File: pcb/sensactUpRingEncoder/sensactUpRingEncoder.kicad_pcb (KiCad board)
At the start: 2 copper layers, 45.7 x 39.5 mm, 60 parts, among them J2 IO35, J3 IO36, J32 PROG, J4 ToBase, J6 USB, Q1 IRLML0030, SW4 RESET, U1 ESP32-S3-MINI-1, U12 AHT20, U2 MAX98357A_WLP_Package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

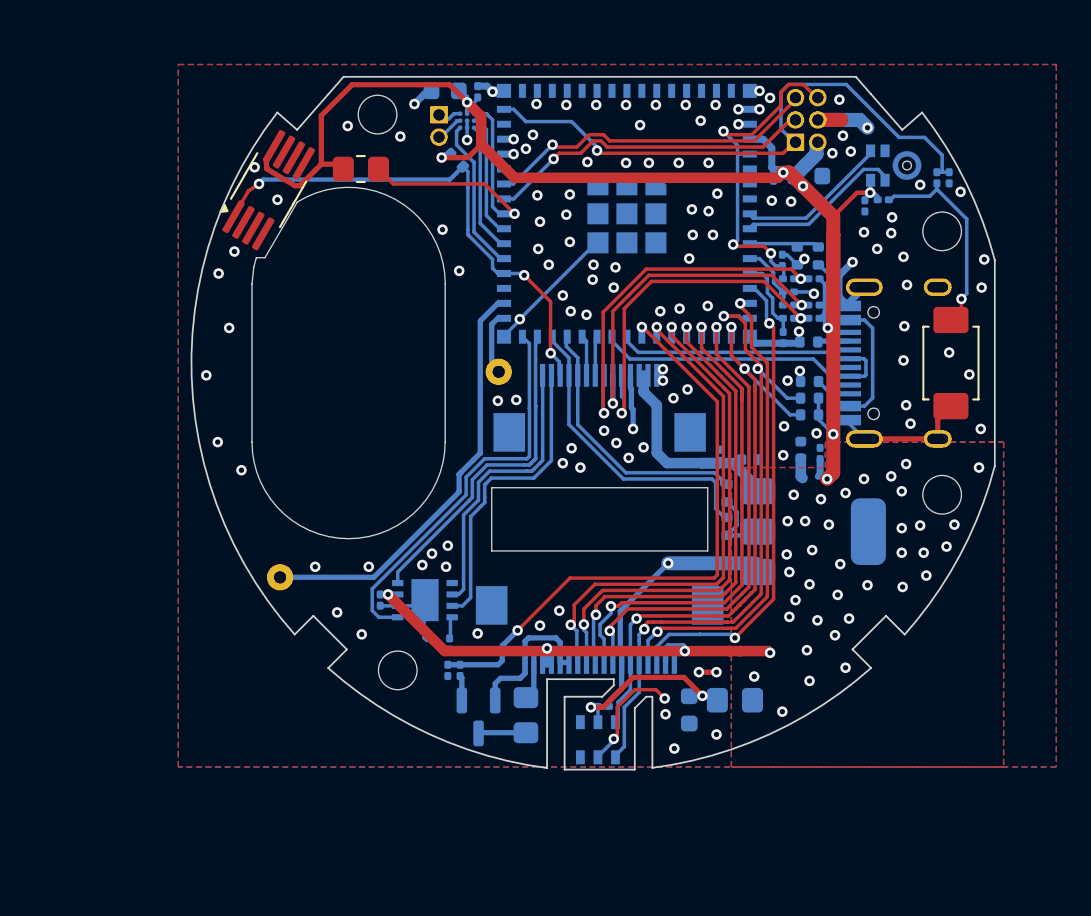
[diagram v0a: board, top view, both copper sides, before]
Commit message: Layout Improvements, added VCML4040
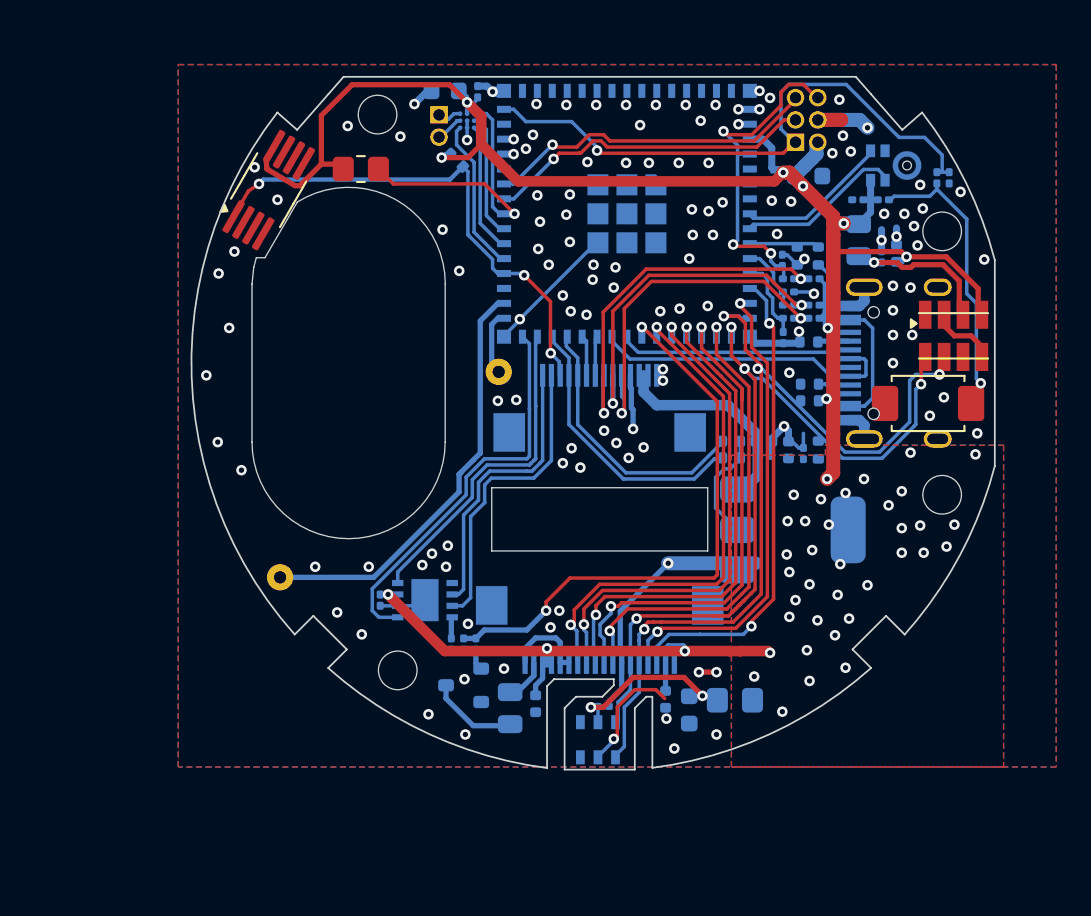
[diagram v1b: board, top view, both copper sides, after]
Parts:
- added C13: 10u, Capacitor_SMD:C_0402_1005Metric, B.Cu at (103.8, 119.2)
- added C14: 10u, Capacitor_SMD:C_0402_1005Metric, B.Cu at (96.3, 119.4)
- added C15: 10u, Capacitor_SMD:C_0402_1005Metric, B.Cu at (116.9, 93.8)
- added C46: u1, Capacitor_SMD:C_0201_0603Metric, B.Cu at (116.0, 94.0)
- added R3: 22R, Resistor_SMD:R_0805_2012Metric, B.Cu at (114.8, 93.0)
- added U5: VCNL4040, liebler_SENSORS:VCNL4040_handsolder, F.Cu at (120.2, 98.5)
- Q1: footprint Package_TO_SOT_SMD:SOT-23 -> liebler_SEMICONDUCTORS:SOT-23_smaller
- R2: value 100R -> 22R; footprint Resistor_SMD:R_0805_2012Metric_Pad1.20x1.40mm_HandSolder -> Resistor_SMD:R_0805_2012Metric
- moved R53 3.91 mm to (107.5, 105.4), turned to 0 degrees
- moved R52 2.96 mm to (107.5, 104.5), turned to 0 degrees
- moved SW4 2.64 mm to (118.7, 102.3), turned to 180 degrees
- moved C10 2.50 mm to (109.4, 105.3), turned to 0 degrees
- moved R51 2.06 mm to (112.5, 105.0), turned to -90 degrees
- moved Q1 1.99 mm to (92.2, 118.3), turned to 180 degrees
- moved R17 1.75 mm to (93.0, 116.0)
- moved R8 1.75 mm to (92.2, 116.0)
- moved C9 1.32 mm to (109.3, 104.5)
- moved U4 1.15 mm to (111.0, 109.5)
- moved R2 0.98 mm to (94.9, 119.7)
- moved C11 0.95 mm to (111.6, 105.2)
- moved C12 0.70 mm to (110.8, 105.0)
- moved C40 0.53 mm to (114.7, 90.7), turned to 180 degrees
- moved R15 0.15 mm to (112.0, 101.2)
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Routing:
- net SDA: track 37.3 -> 51.0 mm, vias 3 -> 4
- net +3V3: track 116.4 -> 129.7 mm, vias 48 -> 47
- net SCL: track 34.3 -> 46.2 mm, vias 3 -> 4
- net Net-(U5-VDD): track 0.00 -> 8.53 mm, vias 0 -> 1
- net GND: track 72.8 -> 65.1 mm
- net Net-(R47-Pad1): track 10.9 -> 15.3 mm
- net Net-(U5-LED_K): track 0.00 -> 2.65 mm
- net Net-(Q1-D): track 2.66 -> 5.04 mm
- net LCD_BL: track 34.4 -> 32.7 mm
- net SDA_EXT: track 17.1 -> 15.7 mm
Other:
- outline, holes or cut-outs redrawn

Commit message: Various updates in sensactRingEncoder
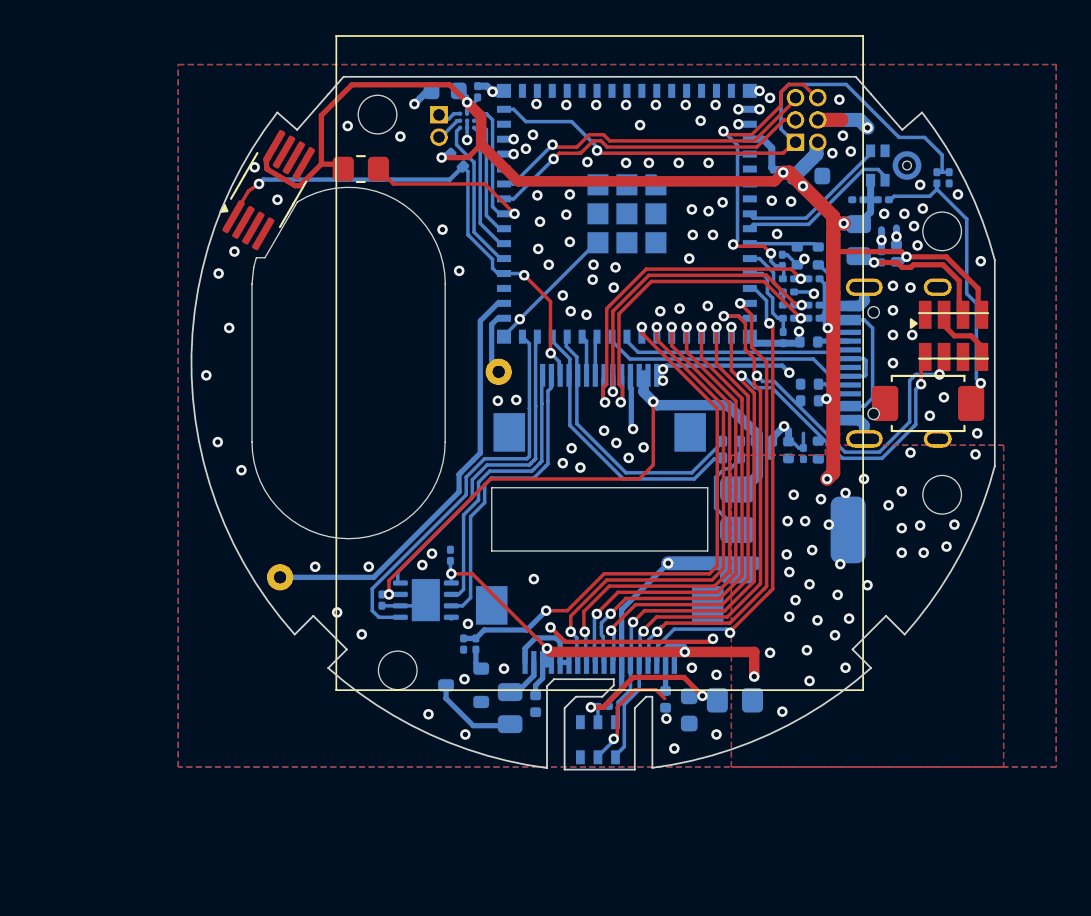
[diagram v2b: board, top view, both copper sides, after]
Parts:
- removed R10: 10k, Resistor_SMD:R_0201_0603Metric
- removed U3: SIT3051TK, Package_DFN_QFN:DFN-8-1EP_3x3mm_P0.65mm_EP1.55x2.4mm
- added C1: u1, Capacitor_SMD:C_0201_0603Metric, B.Cu at (87.6, 113.5)
- added U7: TJA1051TK-3, Package_SON:HVSON-8-1EP_3x3mm_P0.65mm_EP1.6x2.4mm, B.Cu at (90.1, 113.5)
- LS1: value Speaker_withoutTerminals -> Speaker (Mech)
- U2: footprint Package_BGA:WLP-9_1.468x1.448mm_Layout3x3_P0.4mm -> Package_BGA:Maxim_WLP-9_1.595x1.415_Layout3x3_P0.4mm_Ball0.27mm_Pad0.25mm_NSMD
- moved C39 4.74 mm to (91.5, 111.0), turned to 90 degrees
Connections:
- MK1 pad 3_1: (no net) -> GND
- MK1 pad 3_2: (no net) -> GND
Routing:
- net +5V: track 12.0 -> 35.3 mm, vias 0 -> 2
- net GND: track 65.1 -> 81.2 mm, vias 128 -> 127
- net +3V3: track 129.7 -> 127.4 mm
- net /B: track 19.2 -> 17.8 mm
- net Net-(U3-Rs): track 1.23 -> 0.00 mm
- net /A: track 20.3 -> 19.2 mm
- net /S: track 21.2 -> 20.1 mm
- net LCD_DAT: track 28.2 -> 27.2 mm
- net LCD_BL: track 32.7 -> 32.1 mm
- net SDA: track 51.0 -> 50.4 mm
- net LCD_SCK: track 28.1 -> 27.6 mm

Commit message: Various improvements
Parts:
- added J1: IO4, TestPoint:TestPoint_THTPad_D1.0mm_Drill0.5mm, B.Cu at (110.6, 91.9)
- J32: footprint Connector_PinHeader_1.27mm:PinHeader_2x03_P1.27mm_Vertical -> Connector_PinHeader_1.27mm:PinHeader_2x03_P1.27mm_Vertical_SMD
- R1: moved to B.Cu
- moved U6 40.4 mm to (119.5, 102.8), turned to 0 degrees
- moved C38 27.3 mm to (93.1, 84.4), turned to 90 degrees
- moved R46 21.8 mm to (113.2, 93.0), turned to 90 degrees
- moved R48 20.9 mm to (118.6, 110.3)
- moved R47 19.7 mm to (117.8, 110.3), turned to 90 degrees
- moved H4 18.4 mm to (69.0, 85.2)
- moved H3 12.0 mm to (83.6, 128.4)
- moved SW4 10.2 mm to (117.7, 112.5), turned to -126 degrees
- moved J3 7.38 mm to (87.8, 116.5)
- moved R1 6.47 mm to (92.5, 87.0), turned to -90 degrees
- moved C41 3.83 mm to (89.7, 86.4)
- moved U2 2.62 mm to (90.5, 88.0)
- moved Q1 2.51 mm to (90.2, 116.9)
- moved LS3 2.40 mm to (88.5, 86.4)
- moved R2 2.40 mm to (93.5, 117.7), turned to 0 degrees
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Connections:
- R46 pad 1: Onewire -> Onewire_intern
- U1 pad 5: unconnected-(U1-IO1-Pad5) -> MIC_DAT
- U1 pad 6: unconnected-(U1-IO2-Pad6) -> MIC_CLK
- U1 pad 8: MIC_DAT -> Net-(J1-Pin_1)
- U1 pad 9: MIC_CLK -> Onewire_intern
- U6 pad 1: Onewire -> Onewire_intern
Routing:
- net GND: track 81.2 -> 119.1 mm, vias 127 -> 102
- net Onewire: track 27.1 -> 7.77 mm, vias 3 -> 2
- net Onewire_intern: track 0.00 -> 16.9 mm, vias 0 -> 1
- net PROG_EN: track 34.2 -> 50.7 mm, vias 1 -> 3
- net Net-(R47-Pad1): track 15.3 -> 2.05 mm
- net AMP_SD: track 16.0 -> 5.65 mm, vias 1 -> 0
- net +3V3: track 127.4 -> 122.9 mm, vias 47 -> 43
- net Net-(J1-Pin_1): track 0.00 -> 2.30 mm
- net SDA: track 50.4 -> 48.1 mm
- net Net-(U5-LED_K): track 2.65 -> 4.07 mm
- net Net-(Q1-D): track 5.04 -> 3.72 mm
- net SCL: track 45.8 -> 46.9 mm
- net Net-(X1-LEDK): track 1.95 -> 2.97 mm
- net Net-(J6-VBUS-PadA4): track 11.4 -> 12.4 mm
- net PROG_TX: track 18.5 -> 19.5 mm, vias 1 -> 2
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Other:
- board size 45.7 x 39.5 mm -> 44.6 x 39.9 mm

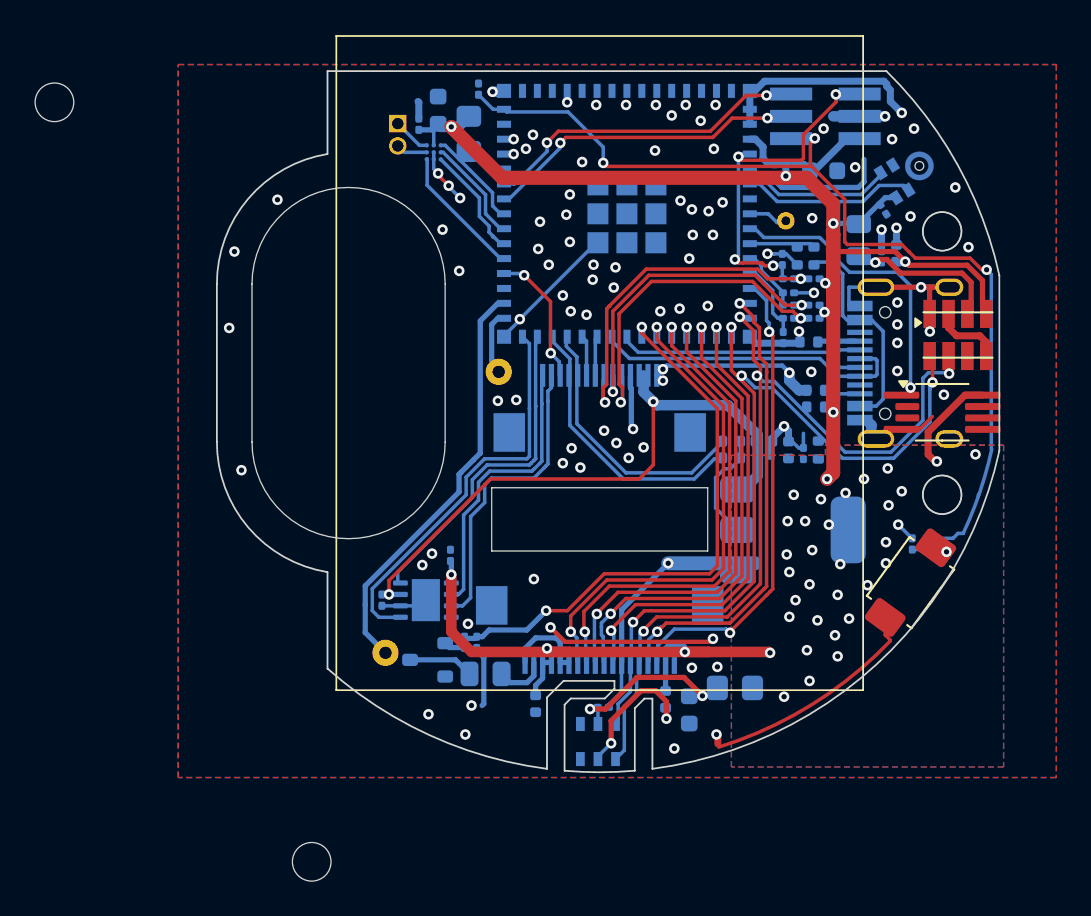
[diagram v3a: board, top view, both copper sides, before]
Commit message: sensactRingEncoder as ordered @ JLCPCB
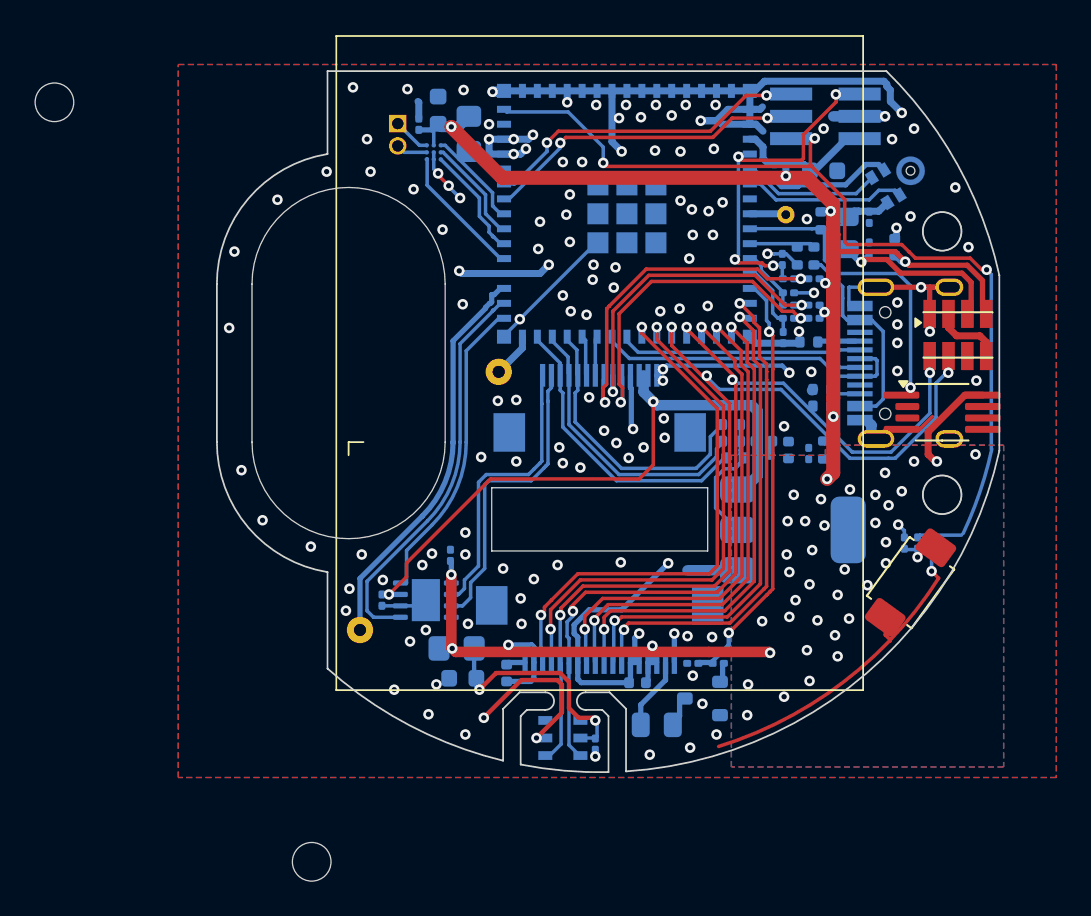
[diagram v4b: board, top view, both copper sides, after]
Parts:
- added R10: 3k3, Resistor_SMD:R_0402_1005Metric, B.Cu at (107.7, 105.4)
- J2: value IO35 -> IO48
- J3: value IO36 -> IO37
- Q1: value IRLML0030 -> AO3400
- R46: value 1k -> 3k3
- X1: footprint Connector_FFC-FPC:Hirose_FH12-18S-0.5SH_1x18-1MP_P0.50mm_Horizontal -> liebler_OPTO:Display_P169H002-CTP
- moved C38 36.5 mm to (118.8, 110.2), turned to -90 degrees
- moved R9 16.0 mm to (91.8, 116.2), turned to 0 degrees
- moved Q1 15.8 mm to (105.8, 119.1)
- moved R17 14.5 mm to (106.8, 117.1), turned to 0 degrees
- moved C56 13.0 mm to (92.2, 118.0), turned to 180 degrees
- moved R8 12.4 mm to (105.3, 117.1), turned to 0 degrees
- moved R2 10.2 mm to (103.2, 120.6), turned to 180 degrees
- moved R51 2.51 mm to (112.7, 102.5), turned to 0 degrees
- moved R50 2.49 mm to (112.8, 105.0), turned to -90 degrees
- moved C14 2.41 mm to (94.7, 117.7), turned to 90 degrees
- moved C57 2.15 mm to (99.8, 121.7), turned to 90 degrees
- moved U12 2.01 mm to (97.9, 121.3), turned to 180 degrees
- moved J3 1.95 mm to (86.3, 115.2)
- moved C13 1.86 mm to (102.2, 118.2), turned to 180 degrees
- moved R46 1.30 mm to (112.6, 91.9)
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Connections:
- U1 pad 13: LCD_TINT -> LCD_BL
- U1 pad 14: LCD_TRST -> LCD_RS
- U1 pad 15: SDA -> LCD_CS
- U1 pad 16: SCL -> LCD_SCK
- U1 pad 17: LCD_RESET -> LCD_DAT
- U1 pad 18: LCD_DAT -> LCD_RESET
- U1 pad 19: LCD_SCK -> SCL
- U1 pad 20: LCD_CS -> SDA
- U1 pad 21: LCD_RS -> LCD_TRST
- U1 pad 22: LCD_BL -> LCD_TINT
- U1 pad 29: CAN_RX -> Onewire
- U1 pad 30: CAN_TX -> Net-(J2-Pin_1)
- U1 pad 31: Net-(J2-Pin_1) -> CAN_RX
- U1 pad 32: Net-(J3-Pin_1) -> CAN_TX
- U1 pad 33: unconnected-(U1-IO37-Pad33) -> Net-(J3-Pin_1)
- U1 pad 34: Onewire -> GND
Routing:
- net GND: track 119.1 -> 141.5 mm, vias 102 -> 141
- net Onewire: track 7.77 -> 16.6 mm, vias 2 -> 0
- net LCD_BL: track 32.1 -> 24.1 mm
- net SDA: track 48.1 -> 54.9 mm
- net CAN_RX: track 18.5 -> 12.0 mm
- net Net-(J3-Pin_1): track 23.9 -> 18.0 mm
- net SCL: track 46.9 -> 52.4 mm
- net CAN_TX: track 22.5 -> 17.5 mm
- net Net-(U12-VDD): track 10.3 -> 13.7 mm
- net LCD_TINT: track 26.6 -> 30.0 mm
- net LCD_TRST: track 27.3 -> 29.7 mm
- net Net-(U5-VDD): track 8.40 -> 10.3 mm
- net +3V3: track 122.9 -> 124.7 mm, vias 43 -> 49
- net Net-(Q1-D): track 3.72 -> 1.90 mm
- net LCD_RESET: track 26.4 -> 28.2 mm
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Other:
- outline, holes or cut-outs redrawn
